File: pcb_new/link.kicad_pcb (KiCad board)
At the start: 8 copper layers, 153.7 x 88.9 mm, 382 parts, among them IC1 IS31FL3236A-TQLS4-TR, J1 STLINK-V3MINIE, J10 3-2328724-1, J11 68021-204HLF, J13 68021-204HLF, J14 68021-204HLF, J16 68021-204HLF, J18 68021-204HLF, J19 USB4105-GF-A, J2 MEM2061-01-188-00-A, J3 SACC-DSIV-M12MS-5CON-L180, J4 68021-204HLF, J5 68021-204HLF, J6 FFC2B35-10-T, J7 USB4105-GF-A, J8 ARJM11B1-009-AB-EW2, J9 ARJM11B1-009-AB-EW2, Q1 PMV20ENR, Q2 PMV20ENR, Q3 PMV20ENR, SW1 TL6400AF160QJ, U1 STM32F479VGT6, U10 TPS2021D, U11 TPS2021D, U12 LM1085ISX-3.3/NOPB, U13 INA226AIDGSR, U14 NC7SZ86P5X, U2 CAHCT1G14QDBVRQ1, U3 TS3DV416DGGR, U4 W5500, U5 W5500, U6 USB3340-EZK-TR, U7 ADG772BCPZ-1REEL, U8 TPS6734ID, U9 LTC4415EMSE#TRPBF, Y1 ECS-2520SMV-240-FP-TR, Y2 ECS-2520SMV-240-FP-TR, Y3 ECS-TXO-2520MV-250-AN-TR, Y4 ECS-TXO-2520MV-250-AN-TR

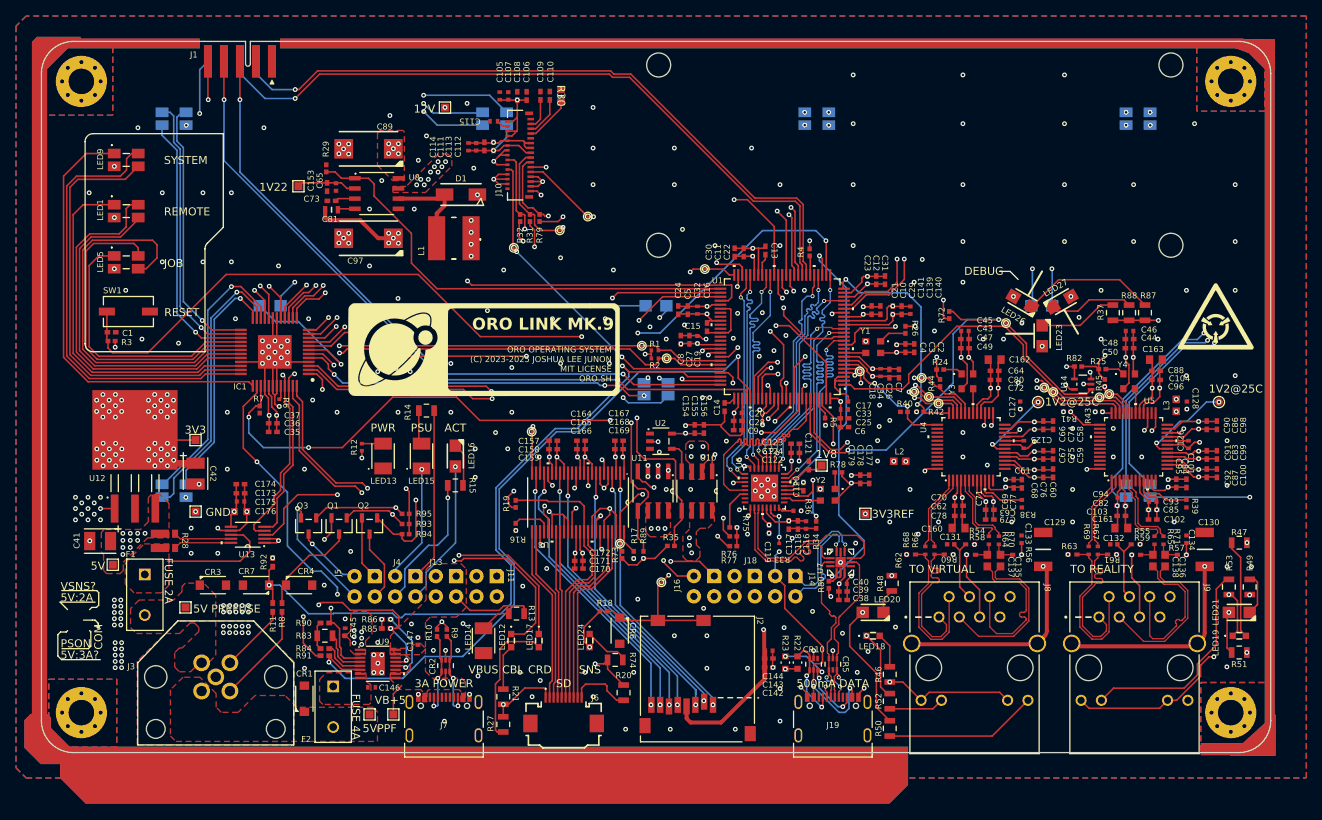
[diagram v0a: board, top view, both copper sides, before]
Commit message: polish link and add atx24 power adapter board
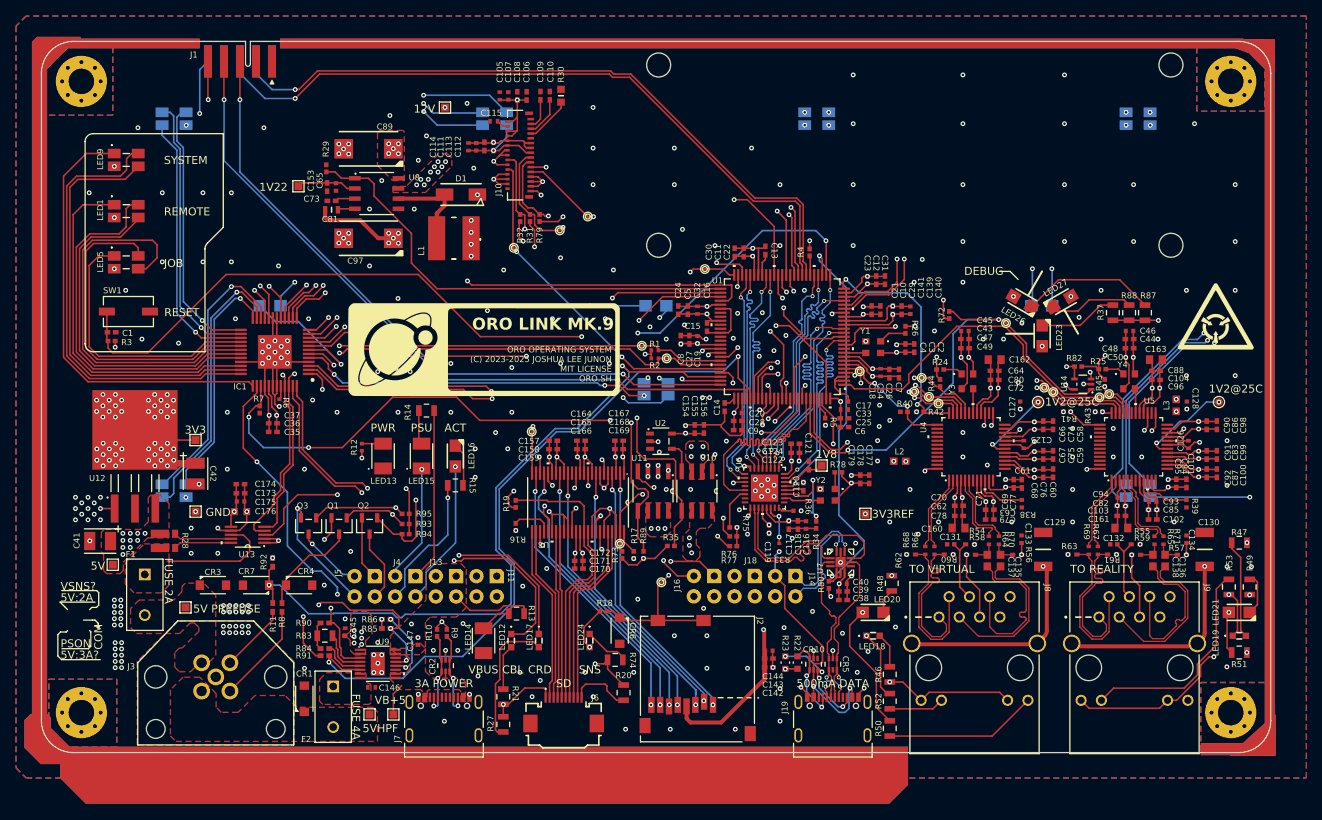
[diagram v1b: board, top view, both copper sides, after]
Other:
- board text added: "5VHPF"
- board text removed: "5VPPF"
